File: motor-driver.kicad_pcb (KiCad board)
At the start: 4 copper layers, 35 x 27 mm, 108 parts, among them J2 SIGNAL, J3 PWR, J4 RTMI, Q4 SIZ322DT, Q5 SIZ322DT, Q6 SIZ322DT, U1 TMC4671, U2 74LVC3G17, U3 74LVC3G17, U4 TMC6200

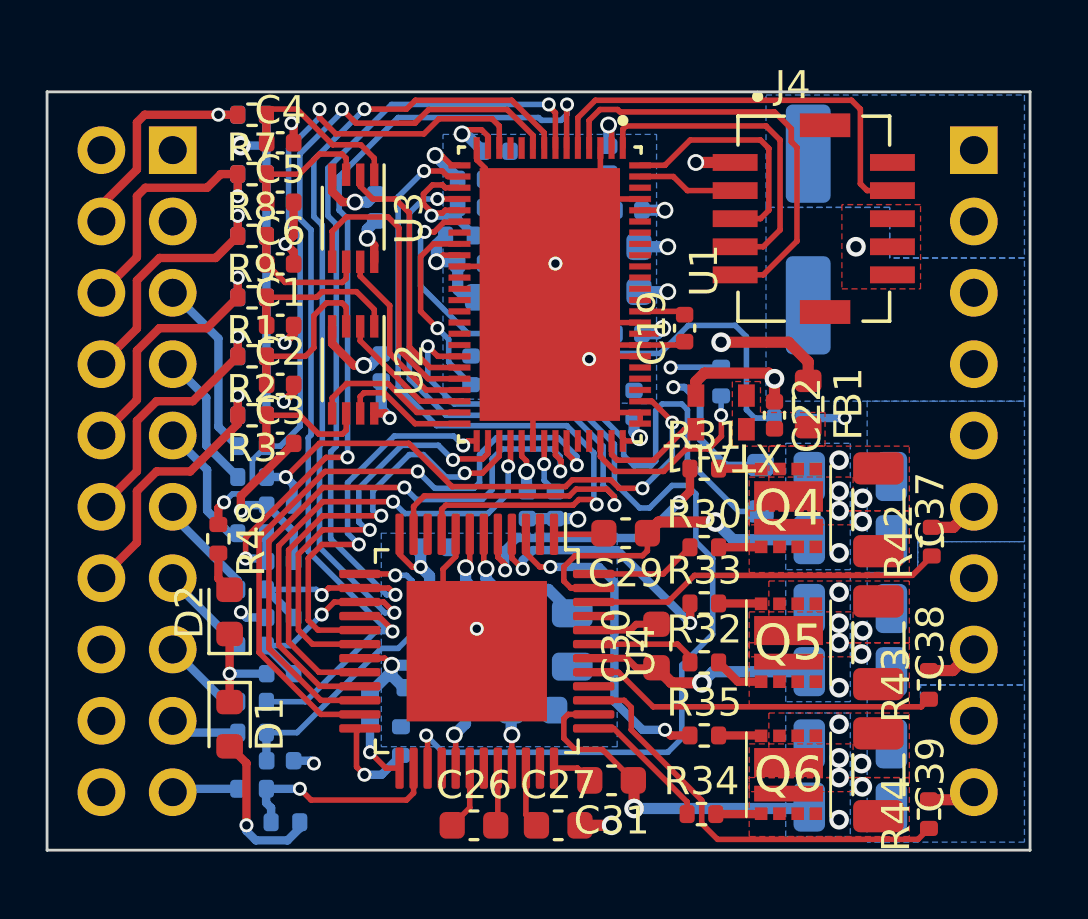
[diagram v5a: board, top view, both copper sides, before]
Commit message: Reroute both main ICs to be able to adhere to the constraints.
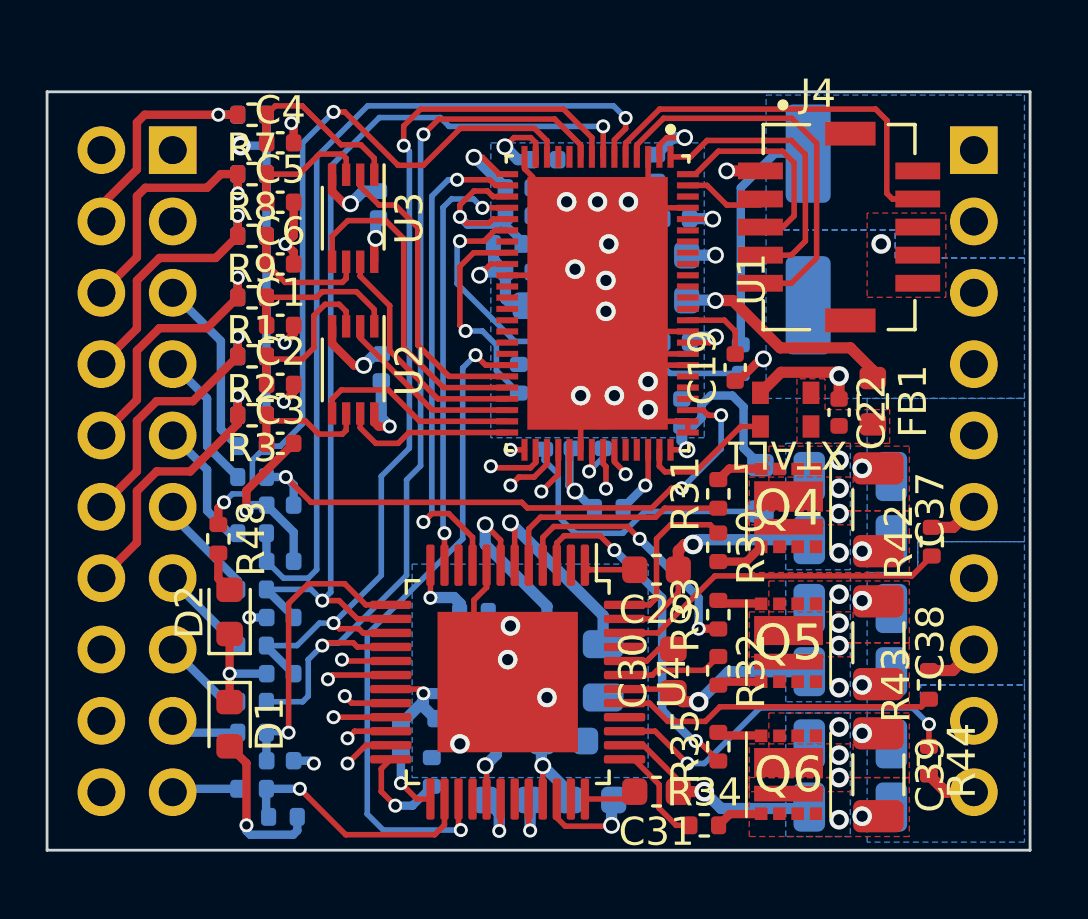
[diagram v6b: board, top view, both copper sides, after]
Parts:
- C26, C27: moved to B.Cu
- moved R13 6.02 mm to (142.9, 91.1), turned to 180 degrees
- moved C20 3.02 mm to (142.7, 88.5), turned to -90 degrees
- moved C16 2.97 mm to (141.6, 88.5), turned to -90 degrees
- moved R18 2.70 mm to (147.6, 85.8), turned to 90 degrees
- moved R16 2.69 mm to (138.1, 94.8)
- moved FB1 2.30 mm to (152.3, 87.3)
- moved XTAL1 2.30 mm to (149.2, 87.6)
- moved C22 2.30 mm to (151.1, 87.7)
- moved C19 2.28 mm to (147.4, 86.1)
- moved R22 2.08 mm to (140.6, 88.5), turned to -90 degrees
- moved R44 1.90 mm to (154.3, 100.1), turned to -90 degrees
- moved U1 1.73 mm to (142.5, 83.8)
- moved C10 1.73 mm to (144.9, 83.7)
- moved C12 1.73 mm to (145.3, 80.8)
- moved C13 1.73 mm to (145.3, 85.2)
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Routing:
- net /CUR_W: track 26.9 -> 15.3 mm
- net /Controller/DRV_EN: track 35.3 -> 23.9 mm
- net /CUR_U: track 25.9 -> 17.9 mm
- net +24V: track 7.85 -> 15.3 mm, vias 10 -> 8
- net +3.3V: track 33.9 -> 39.5 mm, vias 15 -> 12
- net /Controller/ADC_VM: track 20.3 -> 14.8 mm
- net /Controller/WL: track 24.1 -> 18.8 mm
- net Net-(U1-~{RST}): track 7.04 -> 2.44 mm
- net /Driver/W_DRV: track 12.2 -> 7.77 mm
- net /Controller/WH: track 22.4 -> 18.1 mm
- net /Driver/U_DRV: track 11.7 -> 8.62 mm
- net GND: track 39.9 -> 36.8 mm, vias 22 -> 34
- net /SPI_MISO: track 35.7 -> 32.7 mm
- net /~{CS_CTRL}: track 28.5 -> 31.3 mm, vias 3 -> 1
- net Net-(U4-5VOUT): track 4.00 -> 6.83 mm
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
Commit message: Improve routing.
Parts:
- moved R13 2.51 mm to (144.1, 88.9), turned to 0 degrees
- moved R15 1.27 mm to (136.7, 96.3)
- moved R17 0.20 mm to (135.5, 99.1)
- moved TH1 0.14 mm to (148.4, 90.5)
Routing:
- net +3.3V: track 39.5 -> 32.5 mm
- net +24V: track 15.3 -> 8.60 mm
- net +5V: track 16.6 -> 12.8 mm
- net /Controller/WL: track 18.8 -> 20.1 mm
- net Net-(R22-Pad2): track 10.4 -> 9.63 mm
- net Net-(U1-~{RST}): track 2.44 -> 2.96 mm
- added copper zone on B.Cu, net +3.3V
- added copper zone on B.Cu, net +5V

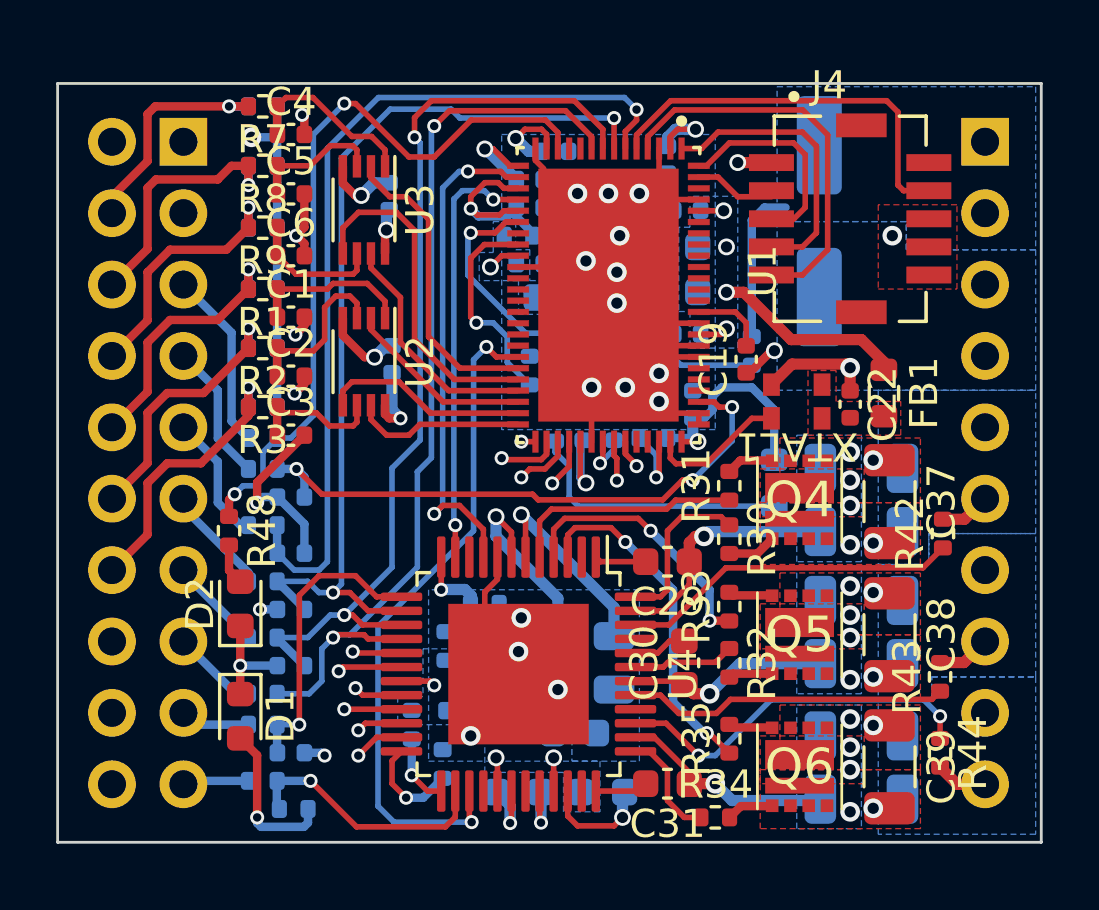
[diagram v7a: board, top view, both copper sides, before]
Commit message: Add teardrops and organized the silkscreens.
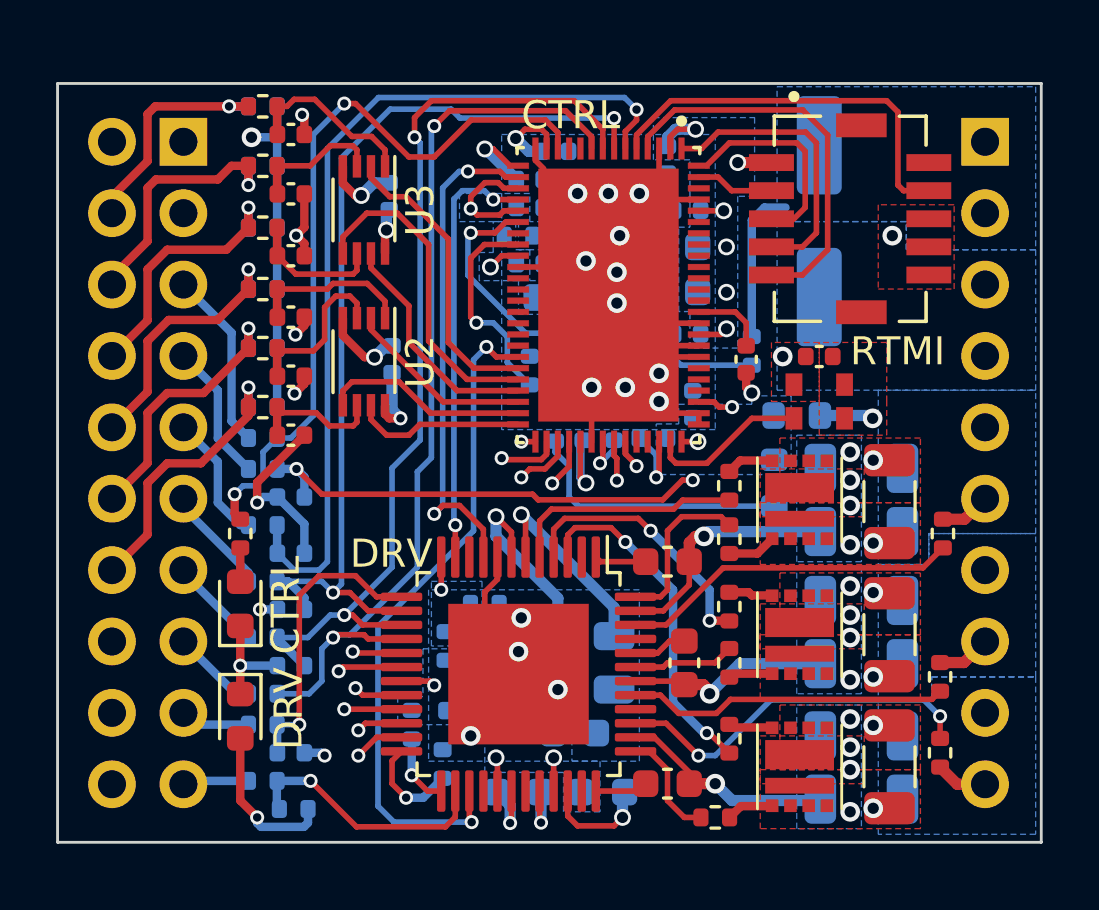
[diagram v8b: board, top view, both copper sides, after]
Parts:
- FB1: moved to B.Cu
- moved FB1 3.20 mm to (149.2, 88.1), turned to 0 degrees
- moved C22 2.02 mm to (150.0, 86.0), turned to 0 degrees
- moved XTAL1 0.80 mm to (150.0, 87.6)
- moved R48 0.41 mm to (129.4, 92.3)
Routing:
- net +3.3V: track 32.5 -> 18.1 mm
- net GND: track 36.8 -> 32.2 mm
- net +2V5: track 8.33 -> 4.24 mm
- net Net-(U4-VOFS/TEST): track 4.54 -> 1.16 mm
- net Net-(XTAL1-EN): track 0.11 -> 1.92 mm, vias 0 -> 1
- net Net-(U1-CLK): track 4.94 -> 5.72 mm
- net +24V: track 8.60 -> 7.91 mm
- net Net-(J2-Pin_17): track 2.49 -> 1.89 mm
- net /ENC_A: track 8.44 -> 7.86 mm
- added copper zone on B.Cu, net +2V5
- added copper zone on B.Cu, net Net-(U4-VOFS/TEST)
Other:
- board text added: "CTRL"
- board text added: "DRV"
- board text added: "RTMI"
- board text added: "V.2023.0.1"
